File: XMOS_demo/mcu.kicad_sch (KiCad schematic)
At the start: 53 parts, among them J1 XSYS2 DEBUG CONNECTOR, U1 U316-1024-QF60B, U2 W25Q32JVSS, Y1 Crystal_24M

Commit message: PCB work
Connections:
- net LED1: now also R2.1, U1.50 (X0D41); no longer R4.1, U1.46 (X0D40)
- net LED2: now also U1.48 (X0D42); no longer U1.50 (X0D41)
- net LED3: now also R4.1, U1.46 (X0D40); no longer R2.1, U1.48 (X0D42)
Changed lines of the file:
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@@
+		)
+	)
+	(label "LED1"
+		(at 250.19 160.02 180)
+		(effects
+			(font
+				(size 1.27 1.27)
+			)
+			(justify right bottom)
 		)
 	)
@@
 		)
 	)
-	(label "LED1"
+	(label "LED3"
 		(at 218.44 154.94 180)
 		(effects
@@
 		)
 	)
-	(label "LED2"
+	(label "LED1"
 		(at 218.44 157.48 180)
 		(effects
@@
 	)
 	(label "LED2"
-		(at 257.81 157.48 180)
-		(effects
-			(font
-				(size 1.27 1.27)
-			)
-			(justify right bottom)
-		)
-	)
-	(label "LED3"
 		(at 218.44 160.02 180)
 		(effects
@@
 		)
 	)
-	(label "LED3"
-		(at 250.19 160.02 180)
-		(effects
-			(font
-				(size 1.27 1.27)
-			)
-			(justify right bottom)
-		)
-	)
 	(label "XTAG_RST_N"
 		(at 132.08 215.9 0)
@@
 		)
 	)
+	(label "LED2"
+		(at 257.81 157.48 180)
+		(effects
+			(font
+				(size 1.27 1.27)
+			)
+			(justify right bottom)
+		)
+	)
 	(label "XTAG_TDI"
 		(at 132.08 220.98 0)
@@
 		)
 	)
-	(label "LED1"
+	(label "LED3"
 		(at 265.43 154.94 180)
 		(effects

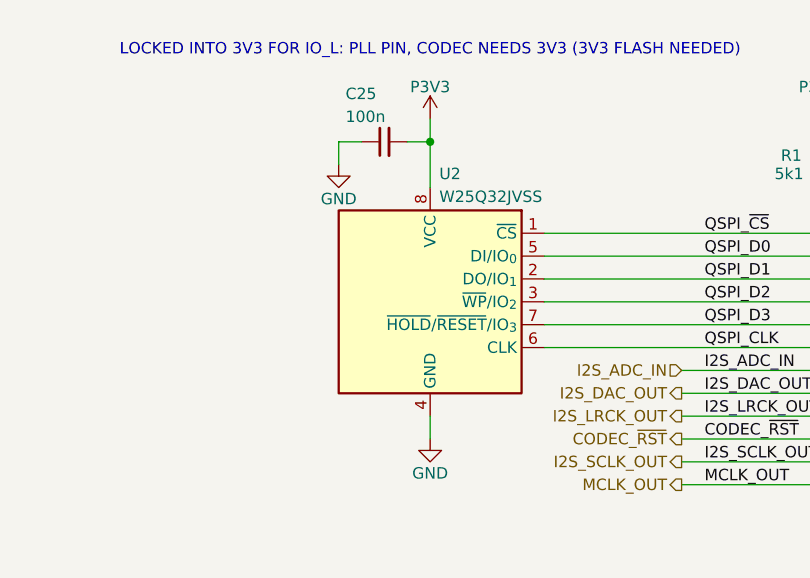
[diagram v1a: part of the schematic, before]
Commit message: Changed flash to correct part
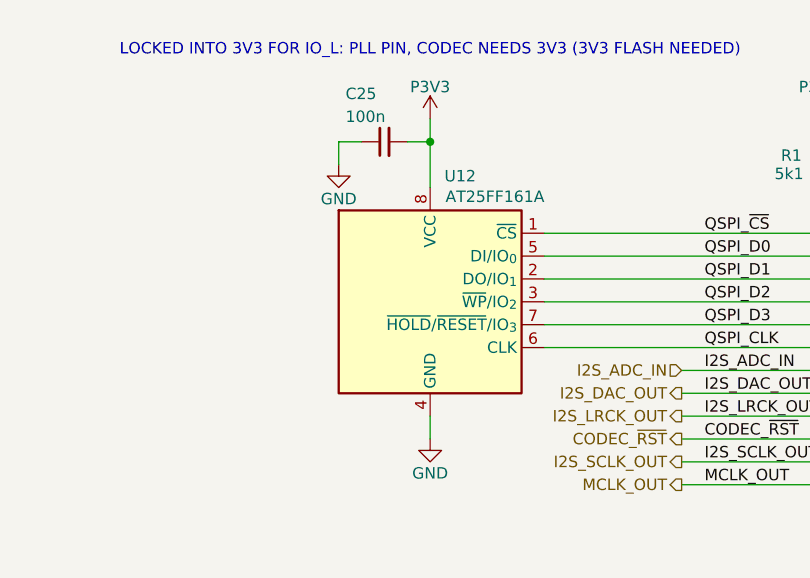
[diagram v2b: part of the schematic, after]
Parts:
- removed U2: W25Q32JVSS, Package_SO:SOIC-8_5.3x5.3mm_P1.27mm, symbol Memory_Flash:W25Q32JVSS
- added U12: AT25FF161A, Package_SO:SOIC-8_5.3x5.3mm_P1.27mm, symbol _Memory_Flash:AT25FF161A
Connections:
- net GND: now also U12.4 (GND)
- net P3V3: now also U12.8 (VCC)
- net QSPI_CLK: now also U12.6 (CLK)
- net QSPI_D0: now also U12.5 (DI/IO_{0})
- net QSPI_D1: now also U12.2 (DO/IO_{1})
- net QSPI_D2: now also U12.3 (~{WP}/IO_{2})
- net QSPI_D3: now also U12.7 (~{HOLD}/~{RESET}/IO_{3})
- net QSPI_~{CS}: now also U12.1 (~{CS})
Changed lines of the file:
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@@
+	)
+	(symbol
+		(lib_id "_Memory_Flash:AT25FF161A")
+		(at 124.46 144.78 0)
+		(unit 1)
+		(exclude_from_sim no)
+		(in_bom yes)
+		(on_board yes)
+		(dnp no)
+		(property "Reference" "U12"
+			(at 142.24 138.43 0)
+			(effects
+				(font
+					(size 1.27 1.27)
+				)
+				(justify right)
+			)
+		)
+		(property "Value" "AT25FF161A"
+			(at 149.86 140.716 0)
+			(effects
+				(font
+					(size 1.27 1.27)
+				)
+				(justify right)
+			)
+		)
+		(property "Footprint" "Package_SO:SOIC-8_5.3x5.3mm_P1.27mm"
+			(at 162.56 171.196 0)
+			(effects
+				(font
+					(size 1.27 1.27)
+				)
+				(hide yes)
+			)
+		)
+		(property "Datasheet" "https://www.renesas.com/en/document/dst/at25ff161a-datasheet?language=en"
+			(at 183.388 173.482 0)
+			(effects
+				(font
+					(size 1.27 1.27)
+				)
+				(hide yes)
+			)
+		)
+		(property "Description" "IC FLASH 16MBIT SPI/QUAD 8SOIC"
+			(at 187.452 176.022 0)
+			(effects
+				(font
+					(size 1.27 1.27)
+				)
+				(hide yes)
+			)
+		)
+		(property "MPN" "AT25FF161A-SHL-T"
+			(at 124.46 144.78 0)
+			(effects
+				(font
+					(size 1.27 1.27)
+				)
+				(hide yes)
+			)
+		)
+		(pin "2"
+		)
+		(pin "5"
+		)
+		(pin "1"
+		)
+		(pin "6"
+		)
+		(pin "3"
+		)
+		(pin "7"
+		)
+		(pin "8"
+		)
+		(pin "4"
+		)
+		(instances
+			(project "XMOS_demo"
+				(path "/0a855fb0-ca19-4770-811e-70d8770d7fdd/e3dab0b8-42bf-48dc-b104-bdc70861b3a4"
+					(reference "U12")
+					(unit 1)
+				)
+			)
+		)
 	)
 	(symbol
@@
 					(unit 1)
 				)
-			)
-		)
-	)
-	(symbol
-		(lib_id "Memory_Flash:W25Q32JVSS")
-		(at 149.86 144.78 0)
-		(mirror y)
-		(unit 1)
-		(exclude_from_sim no)
-		(in_bom yes)
-		(on_board yes)
-		(dnp no)
-		(property "Reference" "U2"
-			(at 138.176 138.176 0)
-			(effects
-				(font
-					(size 1.27 1.27)
-				)
-				(justify right)
-			)
-		)
-		(property "Value" "W25Q32JVSS"
-			(at 138.176 140.716 0)
-			(effects
-				(font
-					(size 1.27 1.27)
-				)
-				(justify right)
-			)
-		)
-		(property "Footprint" "Package_SO:SOIC-8_5.3x5.3mm_P1.27mm"
-			(at 111.76 171.196 0)
-			(effects
-				(font
-					(size 1.27 1.27)
-				)
-				(hide yes)
-			)
-		)
-		(property "Datasheet" "http://www.winbond.com/resource-files/w25q32jv%20revg%2003272018%20plus.pdf"
-			(at 90.932 173.482 0)
-			(effects
-				(font
-					(size 1.27 1.27)
-				)
-				(hide yes)
-			)
-		)
-		(property "Description" "32Mbit / 4MiB Serial Flash Memory, Standard/Dual/Quad SPI, 2.7-3.6V, SOIC-8 (208 mil)"
-			(at 86.868 176.022 0)
-			(effects
-				(font
-					(size 1.27 1.27)
-				)
-				(hide yes)
-			)
-		)
-		(pin "3"
-		)
-		(pin "8"
-		)
-		(pin "7"
-		)
-		(pin "2"
-		)
-		(pin "5"
-		)
-		(pin "4"
-		)
-		(pin "6"
-		)
-		(pin "1"
-		)
-		(instances
-			(project "XMOS_demo"
-				(path "/0a855fb0-ca19-4770-811e-70d8770d7fdd/e3dab0b8-42bf-48dc-b104-bdc70861b3a4"
-					(reference "U2")
-					(unit 1)
-				)
